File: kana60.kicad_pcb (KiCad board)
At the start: 2 copper layers, 285.4 x 115.5 mm, 148 parts, among them SW1 SW_PUSH, SW10 SW_PUSH, SW11 SW_PUSH, SW12 SW_PUSH, SW13 SW_PUSH, SW14 SW_PUSH, SW15 SW_PUSH, SW16 SW_PUSH, SW17 SW_PUSH, SW18 SW_PUSH, SW19 SW_PUSH, SW2 SW_PUSH, SW20 SW_PUSH, SW21 SW_PUSH, SW22 SW_PUSH, SW23 SW_PUSH, SW24 SW_PUSH, SW25 SW_PUSH, SW26 SW_PUSH, SW27 SW_PUSH, SW28 SW_PUSH, SW29 SW_PUSH, SW3 SW_PUSH, SW30 SW_PUSH, SW31 SW_PUSH, SW32 SW_PUSH, SW33 SW_PUSH, SW34 SW_PUSH, SW35 SW_PUSH, SW36 SW_PUSH, SW37 SW_PUSH, SW38 SW_PUSH, SW39 SW_PUSH, SW4 SW_PUSH, SW40 SW_PUSH, SW41 SW_PUSH, SW42 SW_PUSH, SW43 SW_PUSH, SW44 SW_PUSH, SW45 SW_PUSH, SW46 SW_PUSH, SW47 SW_PUSH, SW48 SW_PUSH, SW49 SW_PUSH, SW5 SW_PUSH, SW50 SW_PUSH, SW51 SW_PUSH, SW52 SW_PUSH, SW53 SW_PUSH, SW54 SW_PUSH, SW55 SW_PUSH, SW56 SW_PUSH, SW57 SW_PUSH, SW58 SW_PUSH, SW59 SW_PUSH, SW6 SW_PUSH, SW60 SW_PUSH, SW61 SW_PUSH, SW62 SW_PUSH, SW63 SW_PUSH, SW64 SW_PUSH, SW65 SW_PUSH, SW66 SW_PUSH, SW67 SW_PUSH, SW68 SW_PUSH, SW69 SW_PUSH, SW7 SW_PUSH, SW70 SW_PUSH, SW71 SW_Push, SW8 SW_PUSH, SW9 SW_PUSH, U1 ProMicro

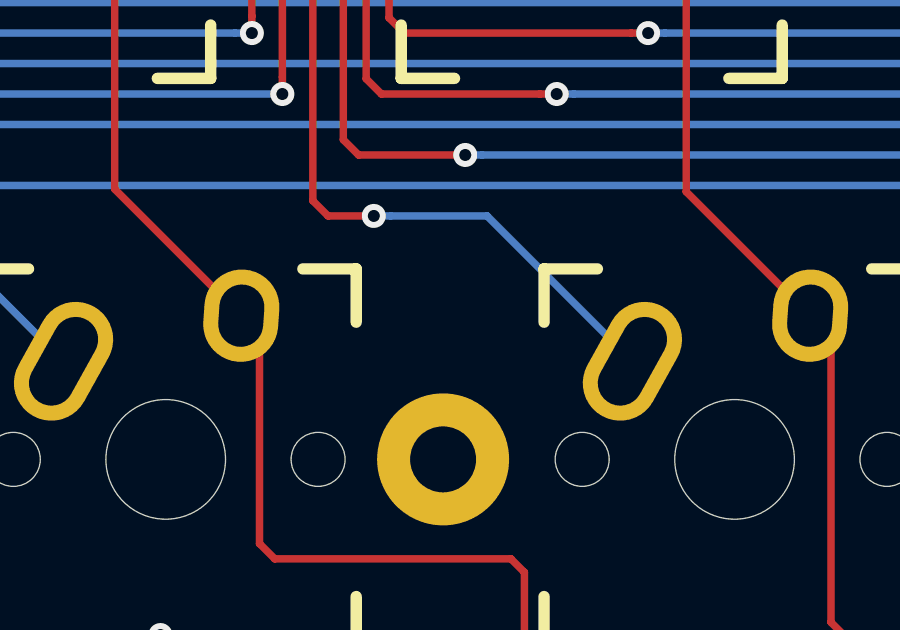
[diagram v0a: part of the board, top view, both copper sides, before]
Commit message: add logo
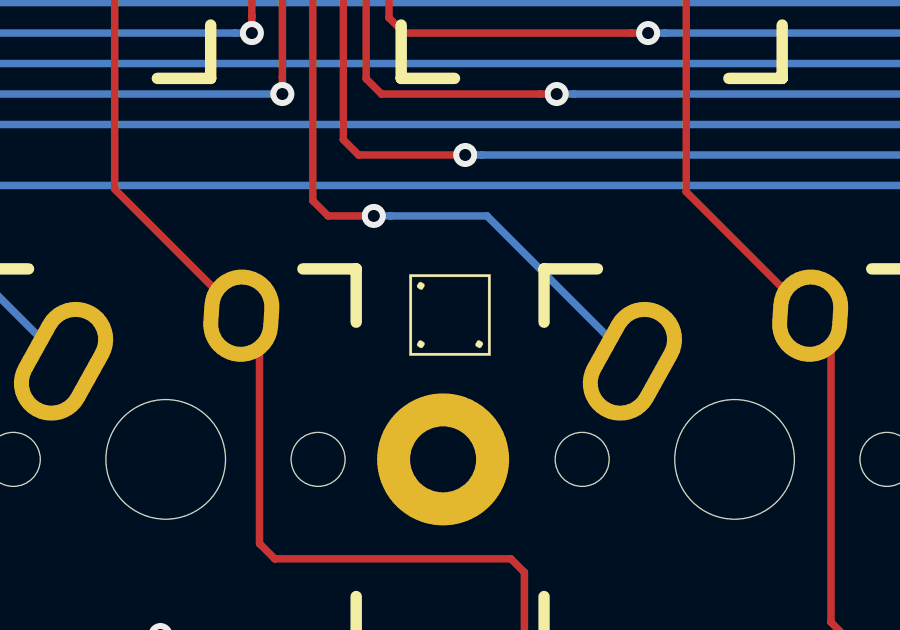
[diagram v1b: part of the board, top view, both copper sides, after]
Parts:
- added G***: LOGO, kana60:sasaplus1-logo, F.Cu at (144.5, 82.5)
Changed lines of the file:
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@@
     (tracks 1095)
     (zones 0)
-    (modules 148)
+    (modules 149)
     (nets 90)
   )
@@
     (add_net GND)
   )
+  (module kana60:sasaplus1-logo (layer F.Cu)
+    (at 144.526 82.55)
+    (fp_text reference G*** (at 0 0) (layer F.SilkS) hide
+      (effects (font (size 1.524 1.524) (thickness 0.3)))
+    )
+    (fp_text value LOGO (at 0.75 0) (layer F.SilkS) hide
+      (effects (font (size 1.524 1.524) (thickness 0.3)))
+    )
+    (fp_poly (pts (xy -0.861418 -1.032894) (xy -0.846666 -0.973666) (xy -0.914439 -0.861418) (xy -0.973666 -0.846666)
+      (xy -1.085915 -0.914439) (xy -1.100666 -0.973666) (xy -1.032894 -1.085915) (xy -0.973666 -1.100666)
+      (xy -0.861418 -1.032894)) (layer F.SilkS) (width 0.01))
+    (fp_poly (pts (xy 1.085915 0.91444) (xy 1.100667 0.973667) (xy 1.032894 1.085915) (xy 0.973667 1.100667)
+      (xy 0.861418 1.032894) (xy 0.846667 0.973667) (xy 0.91444 0.861418) (xy 0.973667 0.846667)
+      (xy 1.085915 0.91444)) (layer F.SilkS) (width 0.01))
+    (fp_poly (pts (xy -0.861418 0.91444) (xy -0.846666 0.973667) (xy -0.914439 1.085915) (xy -0.973666 1.100667)
+      (xy -1.085915 1.032894) (xy -1.100666 0.973667) (xy -1.032894 0.861418) (xy -0.973666 0.846667)
+      (xy -0.861418 0.91444)) (layer F.SilkS) (width 0.01))
+    (fp_poly (pts (xy 1.354667 1.354667) (xy -1.354666 1.354667) (xy -1.354666 -1.27) (xy -1.27 -1.27)
+      (xy -1.27 1.27) (xy 1.27 1.27) (xy 1.27 -1.27) (xy -1.27 -1.27)
+      (xy -1.354666 -1.27) (xy -1.354666 -1.354666) (xy 1.354667 -1.354666) (xy 1.354667 1.354667)) (layer F.SilkS) (width 0.01))
+  )
   (module Keebio-Parts:Hybrid_PCB_100H (layer F.Cu)

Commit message: add title
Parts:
- added G***: LOGO, kana60:kana60-title, B.Cu at (243.3, 74.4)
- added G***: LOGO, kana60:sasaplus1-logo, B.Cu at (67.6, 75.2)
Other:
- board text added: "rev.1.0"

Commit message: update footprint
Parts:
- G*** (x2): footprint kana60:sasaplus1-logo -> kicad-footprints:sasaplus1-icon
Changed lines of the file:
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@@
       (xy -7.044052 1.138264)) (layer B.SilkS) (width 0.01))
   )
-  (module kana60:sasaplus1-logo (layer B.Cu)
+  (module kicad-footprints:sasaplus1-icon (layer B.Cu)
     (at 67.564 75.184 180)
     (fp_text reference G*** (at 0 0) (layer B.SilkS) hide
@@
       (xy -1.354666 1.27) (xy -1.354666 1.354666) (xy 1.354667 1.354666) (xy 1.354667 -1.354667)) (layer B.SilkS) (width 0.01))
   )
-  (module kana60:sasaplus1-logo (layer F.Cu)
+  (module kicad-footprints:sasaplus1-icon (layer F.Cu)
     (at 144.526 82.55)
     (fp_text reference G*** (at 0 0) (layer F.SilkS) hide

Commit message: update footprints
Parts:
- D1, D10, D11, D12, D13, D14, D15, D16, D17, D18, D19, D2, D20, D21, D22, D23, D24, D25, D26, D27, D28, D29, D3, D30, D31, D32, D33, D34, D35, D36, D37, D38, D39, D4, D40, D41, D42, D43, D44, D45, D46, D47, D48, D49, D5, D50, D51, D52, D53, D54, D55, D56, D57, D58, D59, D6, D60, D61, D62, D63, D64, D65, D66, D67, D7, D8, D9: footprint Keebio-Parts:Diode -> kicad-footprints:diode
- SW71: footprint kbd:ResetSW -> kbd:ResetSW_1side

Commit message: move icon position
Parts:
- moved G*** 133.3 mm to (25.7, 22.1)
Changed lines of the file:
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@@
   )
   (module kicad-footprints:sasaplus1-icon (layer F.Cu)
-    (at 144.526 82.55)
+    (at 25.677988 22.0847)
     (fp_text reference G*** (at 0 0) (layer F.SilkS) hide
       (effects (font (size 1.524 1.524) (thickness 0.3)))

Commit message: update PCB
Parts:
- moved G*** 235.0 mm to (260.6, 29.6)
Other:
- board text added: "designed by sasa+1"
- board text removed: "PCB designed by sasa+1"
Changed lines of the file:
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@@
   )
   (module kicad-footprints:sasaplus1-icon (layer F.Cu)
-    (at 25.677988 22.0847)
+    (at 260.607988 29.5747)
     (fp_text reference G*** (at 0 0) (layer F.SilkS) hide
       (effects (font (size 1.524 1.524) (thickness 0.3)))
@@
       (effects (font (size 1.524 1.524) (thickness 0.3)))
     )
-    (fp_poly (pts (xy -0.861418 -1.032894) (xy -0.846666 -0.973666) (xy -0.914439 -0.861418) (xy -0.973666 -0.846666)
-      (xy -1.085915 -0.914439) (xy -1.100666 -0.973666) (xy -1.032894 -1.085915) (xy -0.973666 -1.100666)
-      (xy -0.861418 -1.032894)) (layer F.SilkS) (width 0.01))
-    (fp_poly (pts (xy 1.085915 0.91444) (xy 1.100667 0.973667) (xy 1.032894 1.085915) (xy 0.973667 1.100667)
-      (xy 0.861418 1.032894) (xy 0.846667 0.973667) (xy 0.91444 0.861418) (xy 0.973667 0.846667)
-      (xy 1.085915 0.91444)) (layer F.SilkS) (width 0.01))
-    (fp_poly (pts (xy -0.861418 0.91444) (xy -0.846666 0.973667) (xy -0.914439 1.085915) (xy -0.973666 1.100667)
-      (xy -1.085915 1.032894) (xy -1.100666 0.973667) (xy -1.032894 0.861418) (xy -0.973666 0.846667)
-      (xy -0.861418 0.91444)) (layer F.SilkS) (width 0.01))
     (fp_poly (pts (xy 1.354667 1.354667) (xy -1.354666 1.354667) (xy -1.354666 -1.27) (xy -1.27 -1.27)
       (xy -1.27 1.27) (xy 1.27 1.27) (xy 1.27 -1.27) (xy -1.27 -1.27)
       (xy -1.354666 -1.27) (xy -1.354666 -1.354666) (xy 1.354667 -1.354666) (xy 1.354667 1.354667)) (layer F.SilkS) (width 0.01))
+    (fp_poly (pts (xy -0.861418 0.91444) (xy -0.846666 0.973667) (xy -0.914439 1.085915) (xy -0.973666 1.100667)
+      (xy -1.085915 1.032894) (xy -1.100666 0.973667) (xy -1.032894 0.861418) (xy -0.973666 0.846667)
+      (xy -0.861418 0.91444)) (layer F.SilkS) (width 0.01))
+    (fp_poly (pts (xy 1.085915 0.91444) (xy 1.100667 0.973667) (xy 1.032894 1.085915) (xy 0.973667 1.100667)
+      (xy 0.861418 1.032894) (xy 0.846667 0.973667) (xy 0.91444 0.861418) (xy 0.973667 0.846667)
+      (xy 1.085915 0.91444)) (layer F.SilkS) (width 0.01))
+    (fp_poly (pts (xy -0.861418 -1.032894) (xy -0.846666 -0.973666) (xy -0.914439 -0.861418) (xy -0.973666 -0.846666)
+      (xy -1.085915 -0.914439) (xy -1.100666 -0.973666) (xy -1.032894 -1.085915) (xy -0.973666 -1.100666)
+      (xy -0.861418 -1.032894)) (layer F.SilkS) (width 0.01))
   )
   (module Keebio-Parts:Hybrid_PCB_100H (layer F.Cu)
@@
     (effects (font (size 1 1) (thickness 0.15)) (justify mirror))
   )
-  (gr_text "PCB designed by sasa+1" (at 80.01 75.184) (layer B.SilkS)
+  (gr_text "designed by sasa+1" (at 78.001988 75.1707) (layer B.SilkS)
     (effects (font (size 1 1) (thickness 0.15)) (justify mirror))
   )

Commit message: rewrite Edge.Cuts
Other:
- board size 285.4 x 115.5 mm -> 285.5 x 115.6 mm
